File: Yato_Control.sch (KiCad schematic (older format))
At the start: 14 parts, among them J1 Conn_01x04, J2 Conn_01x04, J3 Conn_01x04, U1 LTV-827, U3 4053

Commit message: initial layout done Signed-off-by: Sir Quickly <sir.quickly0@googlemail.com>
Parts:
- added H1, H2, H3, H4: MountingHole, MountingHole:MountingHole_4mm, symbol Mechanical:MountingHole
- C1: footprint Capacitor_THT:CP_Radial_D10.0mm_P5.00mm -> Capacitor_THT:CP_Radial_D10.0mm_P2.50mm_P5.00mm
- C4: footprint Capacitor_THT:CP_Radial_D10.0mm_P5.00mm -> Capacitor_THT:CP_Radial_D5.0mm_P2.50mm
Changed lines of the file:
@@
 EESchema Schematic File Version 4
-LIBS:first-cache
+LIBS:Yato_Control-cache
 EELAYER 26 0
 EELAYER END
@@
 encoding utf-8
 Sheet 1 1
-Title ""
-Date ""
-Rev ""
-Comp ""
+Title "YATO externe Steuer-Schnittstelle"
+Date "2020-06-05"
+Rev "1.0"
+Comp "#MeBroo (by Roland)"
 Comment1 ""
 Comment2 ""
@@
 F 0 "C1" H 4833 3441 50  0000 R CNN
 F 1 "100uF" H 4833 3350 50  0000 R CNN
-F 2 "Capacitor_THT:CP_Radial_D10.0mm_P5.00mm" H 4988 3200 50  0001 L CNN
+F 2 "Capacitor_THT:CP_Radial_D10.0mm_P2.50mm_P5.00mm" H 4988 3200 50  0001 L CNN
 F 3 "~" H 4950 3350 50  0001 C CNN
 F 4 "6V3" H 4833 3259 50  0000 R CNN "Spannung"
@@
 F 0 "C4" H 8432 4041 50  0000 R CNN
 F 1 "4u7" H 8432 3950 50  0000 R CNN
-F 2 "Capacitor_THT:CP_Radial_D10.0mm_P5.00mm" H 8588 3800 50  0001 C CNN
+F 2 "Capacitor_THT:CP_Radial_D5.0mm_P2.50mm" H 8588 3800 50  0001 C CNN
 F 3 "~" H 8550 3950 50  0001 C CNN
 F 4 "6V3" H 8432 3859 50  0000 R CNN "Spannung"
@@
 Wire Wire Line
 	8550 4200 8550 4300
+$Comp
+L Mechanical:MountingHole H1
+U 1 1 5ED80DD4
+P 1150 7100
+F 0 "H1" H 1250 7146 50  0000 L CNN
+F 1 "MountingHole" H 1250 7055 50  0000 L CNN
+F 2 "MountingHole:MountingHole_4mm" H 1150 7100 50  0001 C CNN
+F 3 "~" H 1150 7100 50  0001 C CNN
+	1    1150 7100
+	1    0    0    -1
+$EndComp
+$Comp
+L Mechanical:MountingHole H2
+U 1 1 5ED80E60
+P 1500 7100
+F 0 "H2" H 1600 7146 50  0000 L CNN
+F 1 "MountingHole" H 1600 7055 50  0000 L CNN
+F 2 "MountingHole:MountingHole_4mm" H 1500 7100 50  0001 C CNN
+F 3 "~" H 1500 7100 50  0001 C CNN
+	1    1500 7100
+	1    0    0    -1
+$EndComp
+$Comp
+L Mechanical:MountingHole H3
+U 1 1 5ED80EE6
+P 1850 7100
+F 0 "H3" H 1950 7146 50  0000 L CNN
+F 1 "MountingHole" H 1950 7055 50  0000 L CNN
+F 2 "MountingHole:MountingHole_4mm" H 1850 7100 50  0001 C CNN
+F 3 "~" H 1850 7100 50  0001 C CNN
+	1    1850 7100
+	1    0    0    -1
+$EndComp
+$Comp
+L Mechanical:MountingHole H4
+U 1 1 5ED80F7E
+P 2250 7100
+F 0 "H4" H 2350 7146 50  0000 L CNN
+F 1 "MountingHole" H 2350 7055 50  0000 L CNN
+F 2 "MountingHole:MountingHole_4mm" H 2250 7100 50  0001 C CNN
+F 3 "~" H 2250 7100 50  0001 C CNN
+	1    2250 7100
+	1    0    0    -1
+$EndComp
 $EndSCHEMATC

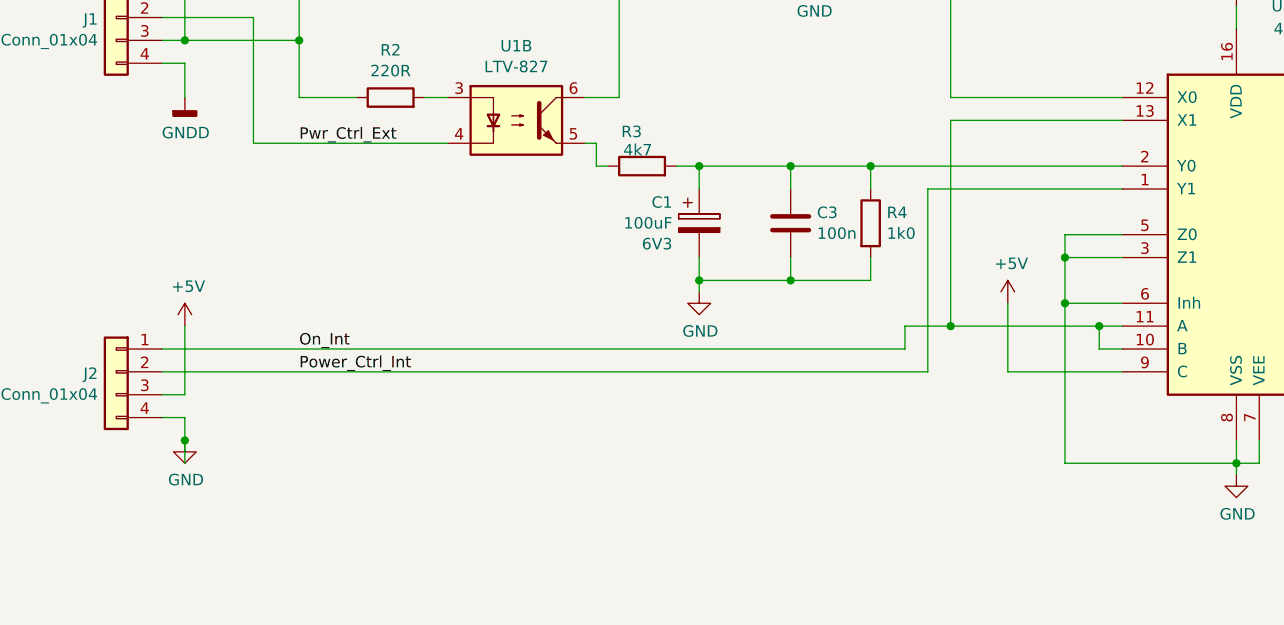
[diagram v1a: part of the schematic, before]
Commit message: - Pulldown Widerstand für das On-Signal von der YATO Poti-Platine - Pos. R4 korrigiert
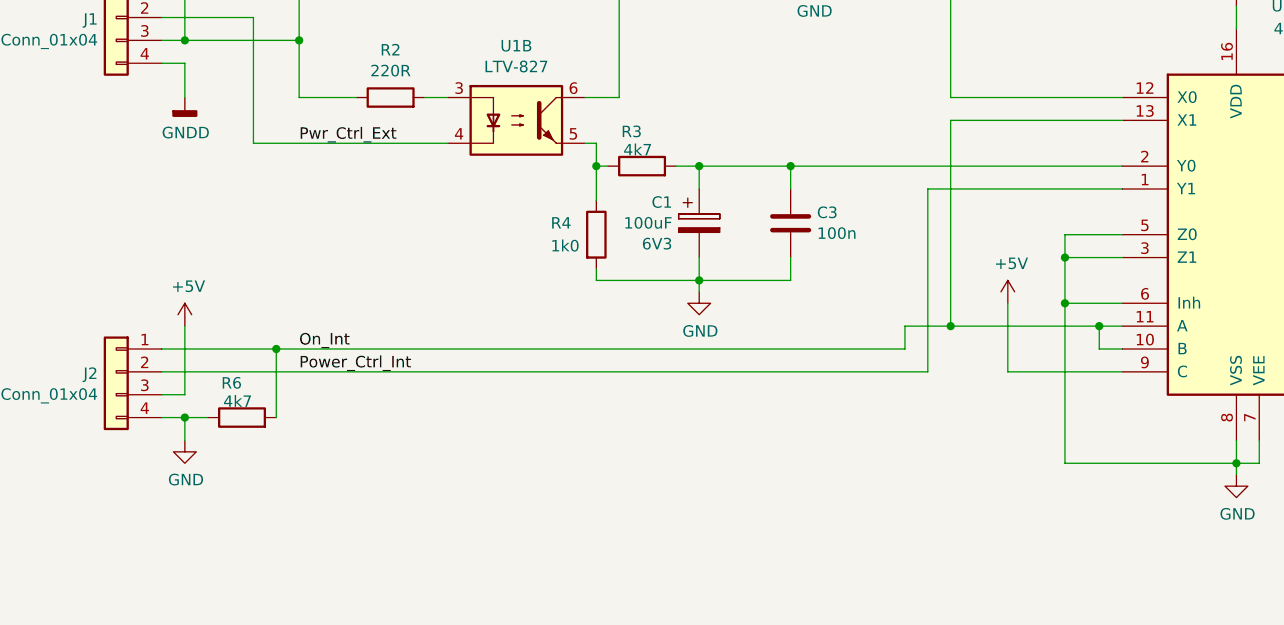
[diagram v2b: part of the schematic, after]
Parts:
- added R6: 4k7, Resistor_THT:R_Axial_DIN0207_L6.3mm_D2.5mm_P7.62mm_Horizontal, symbol Device:R
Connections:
- net GND: now also R6.1
- net On_Int: now also R6.2
- net at C1.1, C3.1, R3.2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: no longer R4.1
- net at R3.1, U1.5: now also R4.1
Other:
- moved on the sheet: R4
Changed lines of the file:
@@
 Pwr_Ctrl_Ext
 Wire Wire Line
-	2600 3900 5850 3900
+	2600 3900 3100 3900
 Wire Wire Line
 	5850 3800 6050 3800
@@
 Wire Wire Line
 	2700 4100 2700 3800
-Connection ~ 2700 4300
-Wire Wire Line
-	2700 4300 2700 4400
 $Comp
 L Device:R R1
@@
 L Device:R R4
 U 1 1 5C8127E9
-P 5700 3350
-F 0 "R4" H 5770 3396 50  0000 L CNN
-F 1 "1k0" H 5770 3305 50  0000 L CNN
-F 2 "Resistor_THT:R_Axial_DIN0207_L6.3mm_D2.5mm_P7.62mm_Horizontal" V 5630 3350 50  0001 C CNN
-F 3 "~" H 5700 3350 50  0001 C CNN
-	1    5700 3350
+P 4500 3400
+F 0 "R4" H 4300 3450 50  0000 L CNN
+F 1 "1k0" H 4300 3350 50  0000 L CNN
+F 2 "Resistor_THT:R_Axial_DIN0207_L6.3mm_D2.5mm_P7.62mm_Horizontal" V 4430 3400 50  0001 C CNN
+F 3 "~" H 4500 3400 50  0001 C CNN
+	1    4500 3400
 	1    0    0    -1
 $EndComp
@@
 Wire Wire Line
 	5850 3900 5850 3800
-Wire Wire Line
-	5700 3500 5700 3600
 Connection ~ 5450 1650
 Wire Wire Line
@@
 	0    -1   -1   0
 $EndComp
-Wire Wire Line
-	5700 3100 6800 3100
-Wire Wire Line
-	5700 3100 5700 3200
 $Comp
 L Device:C C3
@@
 Wire Wire Line
 	5350 3500 5350 3600
-Connection ~ 5350 3600
-Wire Wire Line
-	5350 3600 5700 3600
 Wire Wire Line
 	4950 3200 4950 3100
 Wire Wire Line
 	4950 3100 5350 3100
-Connection ~ 5700 3100
 Wire Wire Line
 	5350 3100 5350 3200
 Connection ~ 5350 3100
-Wire Wire Line
-	5350 3100 5700 3100
 Wire Wire Line
 	4850 3100 4950 3100
@@
 	1    0    0    -1
 $EndComp
+Wire Wire Line
+	5350 3100 6800 3100
+Wire Wire Line
+	4950 3600 4500 3600
+Wire Wire Line
+	4500 3600 4500 3550
+Wire Wire Line
+	4500 3250 4500 3100
+Connection ~ 4500 3100
+$Comp
+L Device:R R6
+U 1 1 5F1A1816
+P 2950 4200
+F 0 "R6" V 3100 4200 50  0000 L CNN
+F 1 "4k7" V 3020 4155 50  0000 L CNN
+F 2 "Resistor_THT:R_Axial_DIN0207_L6.3mm_D2.5mm_P7.62mm_Horizontal" V 2880 4200 50  0001 C CNN
+F 3 "~" H 2950 4200 50  0001 C CNN
+	1    2950 4200
+	0    -1   -1   0
+$EndComp
+Wire Wire Line
+	3100 4200 3100 3900
+Connection ~ 3100 3900
+Wire Wire Line
+	3100 3900 5850 3900
+Wire Wire Line
+	2800 4200 2700 4200
+Connection ~ 2700 4200
 $EndSCHEMATC
